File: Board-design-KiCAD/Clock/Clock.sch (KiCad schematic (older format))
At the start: 54 parts, among them M1 SevSeg4Inch, M2 SevSeg4Inch, Y1 SevSeg1.8Inch, Y2 SevSeg1.8Inch, Y3 SevSeg1.8Inch, Y4 SevSeg1.8Inch

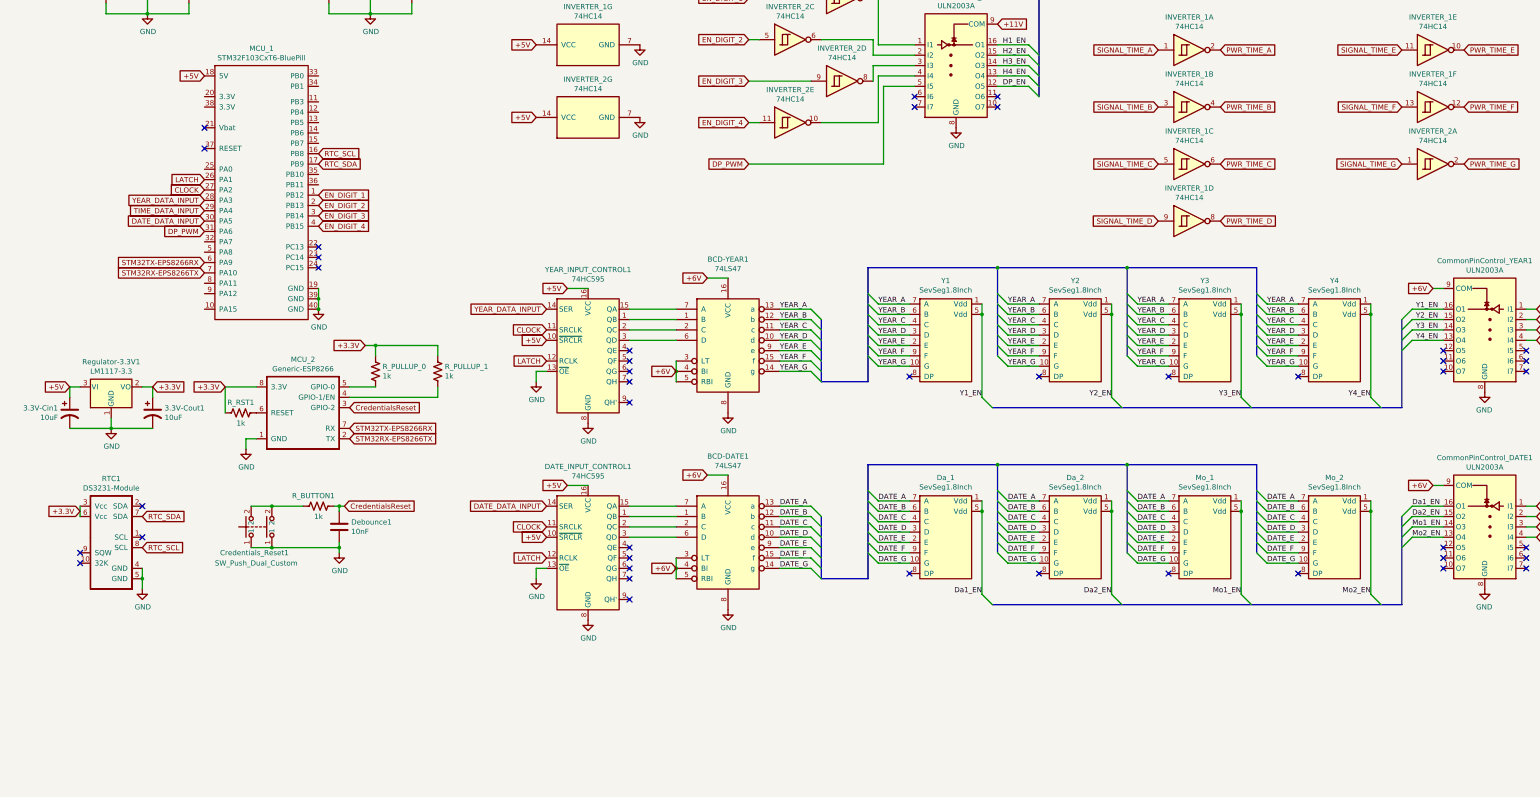
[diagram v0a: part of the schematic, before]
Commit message: Rework on alarm function
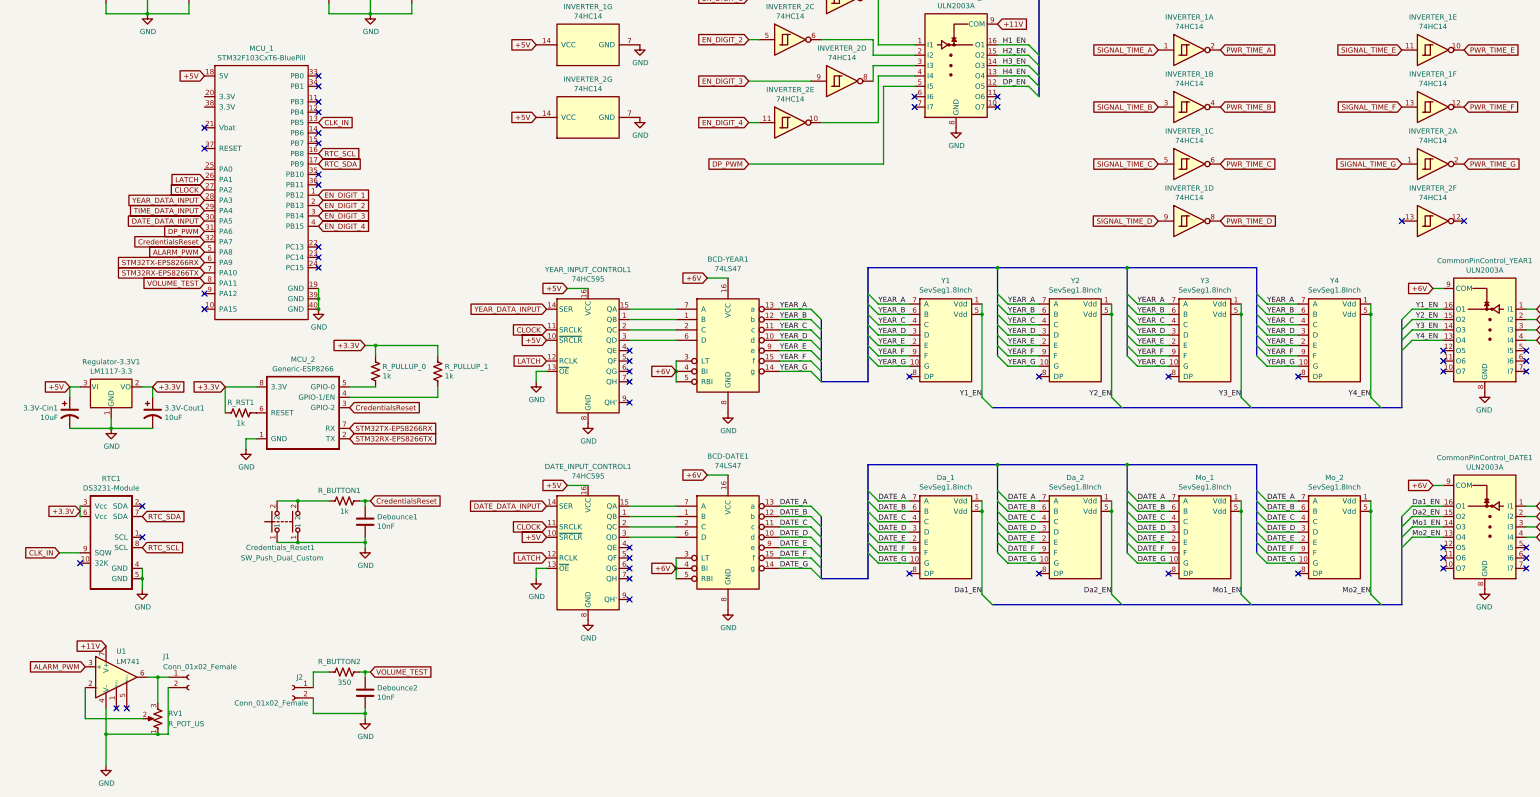
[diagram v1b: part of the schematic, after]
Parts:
- added Debounce2: 10nF, Capacitor_THT:C_Disc_D5.0mm_W2.5mm_P5.00mm, symbol Device:C
- added unit 6 of INVERTER_2
- added J1, J2: Conn_01x02_Female, Connector_PinHeader_2.54mm:PinHeader_1x02_P2.54mm_Vertical, symbol Connector:Conn_01x02_Female
- added RV1: R_POT_US, Potentiometer_THT:Potentiometer_Piher_T-16H_Single_Horizontal, symbol Device:R_POT_US
- added R_BUTTON2: 350, Resistor_THT:R_Axial_DIN0207_L6.3mm_D2.5mm_P10.16mm_Horizontal, symbol Device:R_US
- added U1: LM741, Package_DIP:DIP-8_W7.62mm_Socket_LongPads, symbol Amplifier_Operational:LM741
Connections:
- net +11V: now also U1.7 (V+)
- net CredentialsReset: now also MCU_1.32 (PA7)
- net GND: now also Debounce2.2, J1.2 (Pin_2), J2.2 (Pin_2), RV1.1, U1.4 (V-)
- net CLK_IN: now reaches RTC1.9 (SQW)
- net CLK_IN: now also MCU_1.13 (PB5)
- net ALARM_PWM: now reaches MCU_1.5 (PA8)
- net ALARM_PWM: now also U1.3 (+)
- net VOLUME_TEST: now reaches MCU_1.8 (PA11)
- net VOLUME_TEST: now also Debounce2.1, R_BUTTON2.2
- new net: RV1.2, U1.2 (-)
- new net: J1.1 (Pin_1), RV1.3, U1.6
- new net: J2.1 (Pin_1), R_BUTTON2.1
- no-connect marks 51 -> 64
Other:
- moved on the sheet: Credentials_Reset1, Debounce1, R_BUTTON1

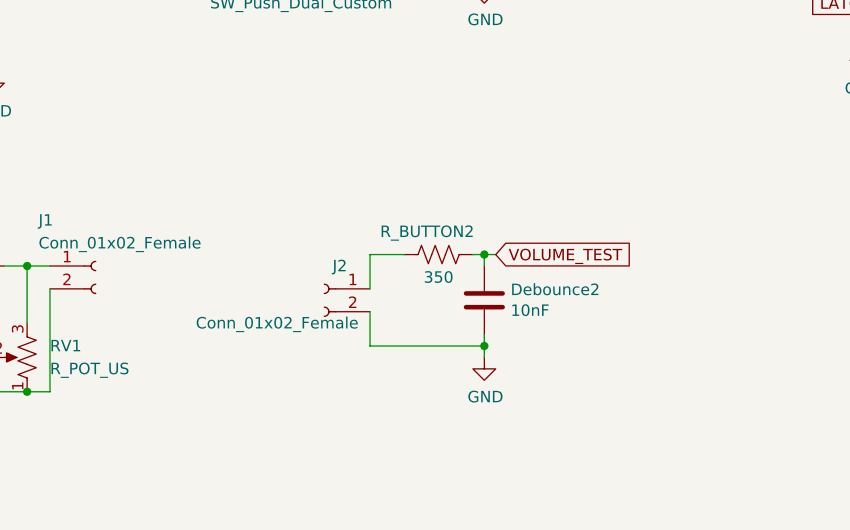
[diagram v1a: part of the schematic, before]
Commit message: Finish up PCB design and fix some minor firmware issue
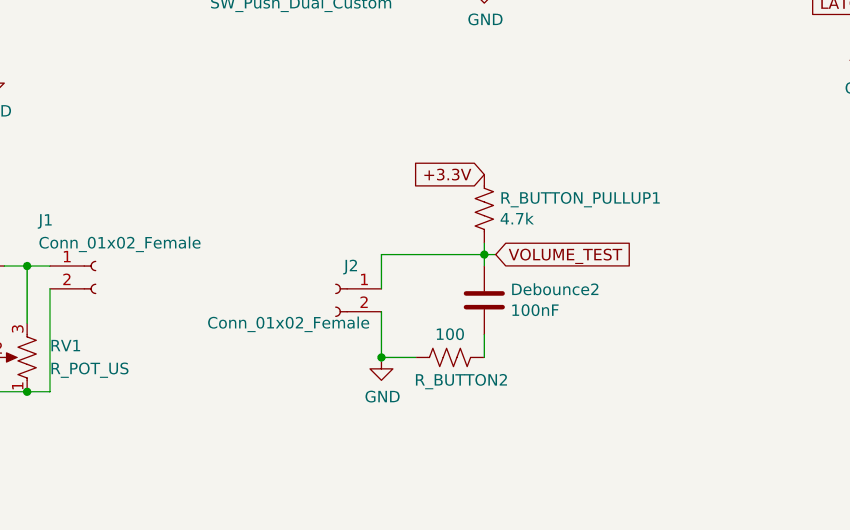
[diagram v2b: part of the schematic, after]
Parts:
- added R_BUTTON_PULLUP1: 4.7k, Resistor_THT:R_Axial_DIN0207_L6.3mm_D2.5mm_P10.16mm_Horizontal, symbol Device:R_US
- Debounce2: value 10nF -> 100nF; footprint Capacitor_THT:C_Disc_D5.0mm_W2.5mm_P5.00mm -> Custom:CP_Radial_H15.0mm_W14.0mm_T8.0mm_P8.5mm_Horizontal
- R_BUTTON2: value 350 -> 100
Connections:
- net +3.3V: now also R_BUTTON_PULLUP1.1
- net GND: now also R_BUTTON2.2; no longer Debounce2.2
- net VOLUME_TEST: now also J2.1 (Pin_1), R_BUTTON_PULLUP1.2; no longer R_BUTTON2.2
- net at R_BUTTON2.1: now also Debounce2.2; no longer J2.1 (Pin_1)
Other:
- moved on the sheet: J2, R_BUTTON2
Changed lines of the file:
@@
 P 3950 9600
 F 0 "Debounce2" H 4065 9646 50  0000 L CNN
-F 1 "10nF" H 4065 9555 50  0000 L CNN
-F 2 "Capacitor_THT:C_Disc_D5.0mm_W2.5mm_P5.00mm" H 3988 9450 50  0001 C CNN
+F 1 "100nF" H 4065 9555 50  0000 L CNN
+F 2 "Custom:CP_Radial_H15.0mm_W14.0mm_T8.0mm_P8.5mm_Horizontal" H 3988 9450 50  0001 C CNN
 F 3 "~" H 3950 9600 50  0001 C CNN
 	1    3950 9600
@@
 L power:GND #PWR0121
 U 1 1 5F971AAE
-P 3950 9850
-F 0 "#PWR0121" H 3950 9600 50  0001 C CNN
-F 1 "GND" H 3955 9677 50  0000 C CNN
-F 2 "" H 3950 9850 50  0001 C CNN
-F 3 "" H 3950 9850 50  0001 C CNN
-	1    3950 9850
+P 3500 9850
+F 0 "#PWR0121" H 3500 9600 50  0001 C CNN
+F 1 "GND" H 3505 9677 50  0000 C CNN
+F 2 "" H 3500 9850 50  0001 C CNN
+F 3 "" H 3500 9850 50  0001 C CNN
+	1    3500 9850
 	1    0    0    -1
 $EndComp
@@
 L Device:R_US R_BUTTON2
 U 1 1 5F971AB4
-P 3750 9400
-F 0 "R_BUTTON2" V 3850 9450 50  0000 C CNN
-F 1 "350" V 3650 9400 50  0000 C CNN
-F 2 "Resistor_THT:R_Axial_DIN0207_L6.3mm_D2.5mm_P10.16mm_Horizontal" V 3790 9390 50  0001 C CNN
-F 3 "~" H 3750 9400 50  0001 C CNN
-	1    3750 9400
-	0    -1   -1   0
+P 3800 9850
+F 0 "R_BUTTON2" V 3900 9900 50  0000 C CNN
+F 1 "100" V 3700 9850 50  0000 C CNN
+F 2 "Resistor_THT:R_Axial_DIN0207_L6.3mm_D2.5mm_P10.16mm_Horizontal" V 3840 9840 50  0001 C CNN
+F 3 "~" H 3800 9850 50  0001 C CNN
+	1    3800 9850
+	0    1    1    0
 $EndComp
-Wire Wire Line
-	3950 9400 3900 9400
 Wire Wire Line
 	3950 9450 3950 9400
@@
 L Connector:Conn_01x02_Female J2
 U 1 1 5F9E34AD
-P 3250 9550
-F 0 "J2" H 3150 9650 50  0000 L CNN
-F 1 "Conn_01x02_Female" H 3100 9400 50  0000 L CNN
-F 2 "Connector_PinHeader_2.54mm:PinHeader_1x02_P2.54mm_Vertical" H 3250 9550 50  0001 C CNN
-F 3 "~" H 3250 9550 50  0001 C CNN
-	1    3250 9550
+P 3300 9550
+F 0 "J2" H 3200 9650 50  0000 L CNN
+F 1 "Conn_01x02_Female" H 3150 9400 50  0000 L CNN
+F 2 "Connector_PinHeader_2.54mm:PinHeader_1x02_P2.54mm_Vertical" H 3300 9550 50  0001 C CNN
+F 3 "~" H 3300 9550 50  0001 C CNN
+	1    3300 9550
 	-1   0    0    -1
 $EndComp
-Wire Wire Line
-	3950 9750 3950 9800
-Wire Wire Line
-	3450 9550 3450 9400
-Wire Wire Line
-	3450 9400 3600 9400
-Wire Wire Line
-	3450 9650 3450 9800
-Wire Wire Line
-	3450 9800 3950 9800
-Connection ~ 3950 9800
-Wire Wire Line
-	3950 9800 3950 9850
 Text GLabel 2400 5650 0    50   Input ~ 0
 VOLUME_TEST
@@
 NoConn ~ 13950 5050
 NoConn ~ 14550 5050
+$Comp
+L Device:R_US R_BUTTON_PULLUP1
+U 1 1 5F9893B5
+P 3950 9200
+F 0 "R_BUTTON_PULLUP1" H 4018 9246 50  0000 L CNN
+F 1 "4.7k" H 4018 9155 50  0000 L CNN
+F 2 "Resistor_THT:R_Axial_DIN0207_L6.3mm_D2.5mm_P10.16mm_Horizontal" V 3990 9190 50  0001 C CNN
+F 3 "~" H 3950 9200 50  0001 C CNN
+	1    3950 9200
+	1    0    0    -1
+$EndComp
+Text GLabel 3950 9050 0    50   Input ~ 0
++3.3V
+Wire Wire Line
+	3950 9350 3950 9400
+Wire Wire Line
+	3500 9550 3500 9400
+Wire Wire Line
+	3500 9400 3950 9400
+Wire Wire Line
+	3500 9650 3500 9850
+Wire Wire Line
+	3500 9850 3650 9850
+Connection ~ 3500 9850
+Wire Wire Line
+	3950 9850 3950 9750
 Wire Bus Line
 	10000 8750 13950 8750

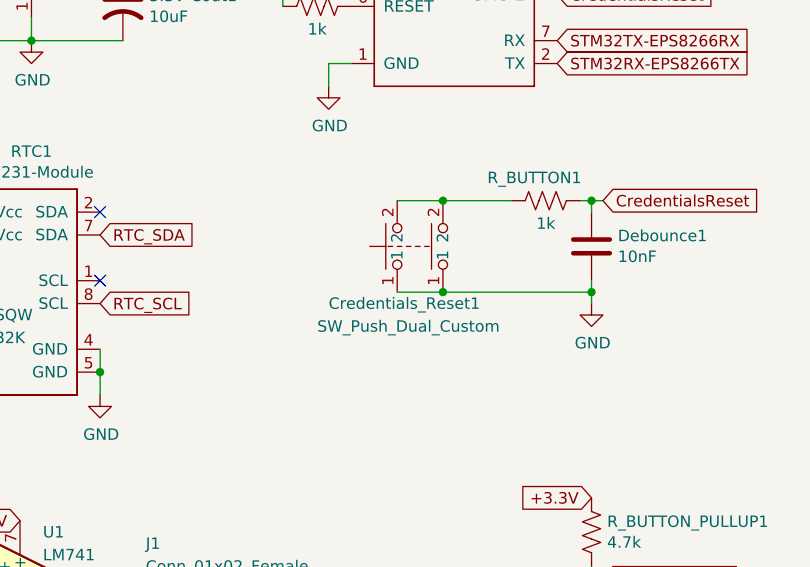
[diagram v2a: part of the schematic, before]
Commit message: Add mounting holes and generate gerber files
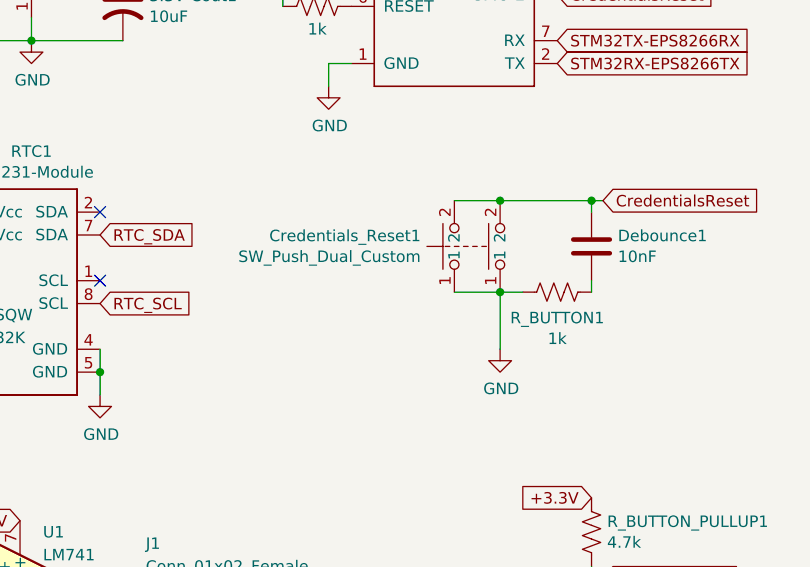
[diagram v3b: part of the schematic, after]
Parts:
- Debounce1: footprint Capacitor_THT:C_Disc_D5.0mm_W2.5mm_P5.00mm -> Custom:CP_Radial_H15.0mm_W14.0mm_T8.0mm_P8.5mm_Horizontal
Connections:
- net CredentialsReset: now also Credentials_Reset1.2; no longer R_BUTTON1.2
- net GND: now also R_BUTTON1.1; no longer Debounce1.2
- new net: Debounce1.2, R_BUTTON1.2
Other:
- moved on the sheet: Credentials_Reset1, R_BUTTON1
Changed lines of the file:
@@
 F 0 "Debounce1" H 4065 7996 50  0000 L CNN
 F 1 "10nF" H 4065 7905 50  0000 L CNN
-F 2 "Capacitor_THT:C_Disc_D5.0mm_W2.5mm_P5.00mm" H 3988 7800 50  0001 C CNN
+F 2 "Custom:CP_Radial_H15.0mm_W14.0mm_T8.0mm_P8.5mm_Horizontal" H 3988 7800 50  0001 C CNN
 F 3 "~" H 3950 7950 50  0001 C CNN
 	1    3950 7950
@@
 L power:GND #PWR0119
 U 1 1 5F765C62
-P 3950 8200
-F 0 "#PWR0119" H 3950 7950 50  0001 C CNN
-F 1 "GND" H 3955 8027 50  0000 C CNN
-F 2 "" H 3950 8200 50  0001 C CNN
-F 3 "" H 3950 8200 50  0001 C CNN
-	1    3950 8200
+P 3550 8400
+F 0 "#PWR0119" H 3550 8150 50  0001 C CNN
+F 1 "GND" H 3555 8227 50  0000 C CNN
+F 2 "" H 3550 8400 50  0001 C CNN
+F 3 "" H 3550 8400 50  0001 C CNN
+	1    3550 8400
 	1    0    0    -1
 $EndComp
@@
 L Device:R_US R_BUTTON1
 U 1 1 5F767A96
-P 3750 7750
-F 0 "R_BUTTON1" V 3850 7800 50  0000 C CNN
-F 1 "1k" V 3650 7750 50  0000 C CNN
-F 2 "Resistor_THT:R_Axial_DIN0207_L6.3mm_D2.5mm_P10.16mm_Horizontal" V 3790 7740 50  0001 C CNN
-F 3 "~" H 3750 7750 50  0001 C CNN
-	1    3750 7750
+P 3800 8150
+F 0 "R_BUTTON1" V 3687 8150 50  0000 C CNN
+F 1 "1k" V 3596 8150 50  0000 C CNN
+F 2 "Resistor_THT:R_Axial_DIN0207_L6.3mm_D2.5mm_P10.16mm_Horizontal" V 3840 8140 50  0001 C CNN
+F 3 "~" H 3800 8150 50  0001 C CNN
+	1    3800 8150
 	0    -1   -1   0
 $EndComp
-Wire Wire Line
-	3950 7750 3900 7750
 Wire Wire Line
 	3950 7800 3950 7750
 Connection ~ 3950 7750
 Connection ~ 3500 5900
-Wire Wire Line
-	3950 8150 3950 8200
-Wire Wire Line
-	3950 8150 3950 8100
-Connection ~ 3950 8150
 Text GLabel 4000 7750 2    50   Input ~ 0
 CredentialsReset
 Wire Wire Line
 	4000 7750 3950 7750
-Wire Wire Line
-	3300 8150 3950 8150
-Wire Wire Line
-	3300 7750 3600 7750
 $Comp
 L Custom:SW_Push_Dual_Custom Credentials_Reset1
 U 1 1 5F9F281E
-P 3150 7950
-F 0 "Credentials_Reset1" V 2900 8300 50  0000 R CNN
-F 1 "SW_Push_Dual_Custom" V 2800 8350 50  0000 R CNN
-F 2 "Button_Switch_THT:SW_PUSH-12mm_Wuerth-430476085716" H 3150 7950 50  0001 C CNN
-F 3 "" H 3150 7950 50  0001 C CNN
-	1    3150 7950
+P 3400 7950
+F 0 "Credentials_Reset1" V 3446 8147 50  0000 L CNN
+F 1 "SW_Push_Dual_Custom" V 3355 8147 50  0000 L CNN
+F 2 "Button_Switch_THT:SW_PUSH-12mm_Wuerth-430476085716" H 3400 7950 50  0001 C CNN
+F 3 "" H 3400 7950 50  0001 C CNN
+	1    3400 7950
 	0    -1   -1   0
 $EndComp
-Wire Wire Line
-	3100 8150 3300 8150
-Connection ~ 3300 8150
-Wire Wire Line
-	3100 7750 3300 7750
-Connection ~ 3300 7750
 Text GLabel 3800 6850 2    50   Input ~ 0
 CredentialsReset
@@
 Wire Wire Line
 	3950 9850 3950 9750
+Wire Wire Line
+	3350 7750 3550 7750
+Wire Wire Line
+	3550 7750 3950 7750
+Connection ~ 3550 7750
+Wire Wire Line
+	3350 8150 3550 8150
+Wire Wire Line
+	3550 8400 3550 8150
+Connection ~ 3550 8150
+Wire Wire Line
+	3550 8150 3650 8150
+Wire Wire Line
+	3950 8150 3950 8100
 Wire Bus Line
 	10000 8750 13950 8750
